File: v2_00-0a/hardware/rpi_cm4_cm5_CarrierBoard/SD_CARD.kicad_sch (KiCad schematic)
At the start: 17 parts, among them J1 DM3AT-SF-PEJM5, Q4 2N7002, Q5 2N7002, Q6 2N7002, U4 AP22913W6-7

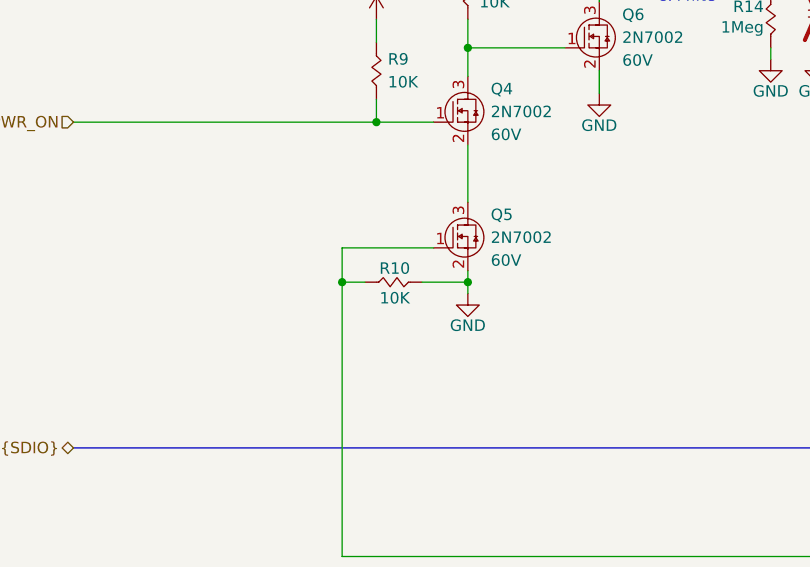
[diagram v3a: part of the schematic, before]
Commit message: Add design notes (power table) and latest changes to power supply and power input
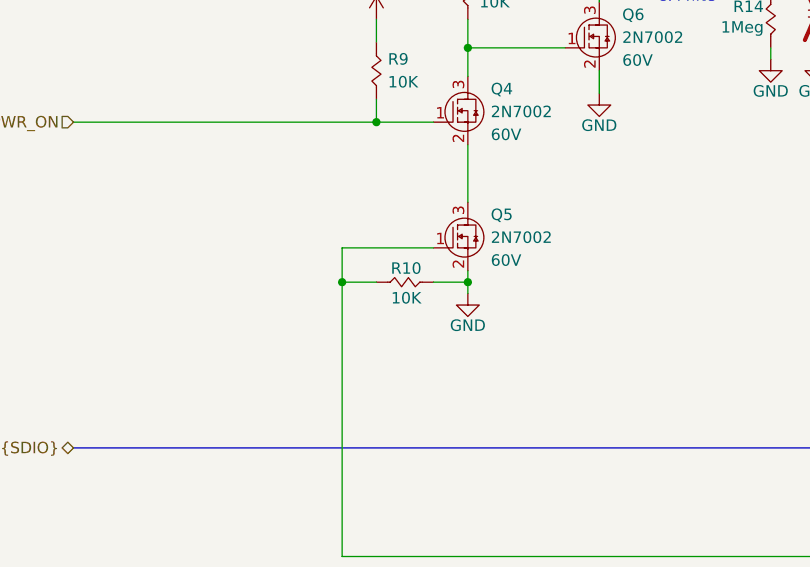
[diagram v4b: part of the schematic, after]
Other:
- moved on the sheet: R10
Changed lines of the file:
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@@
 	(wire
 		(pts
-			(xy 83.185 93.98) (xy 88.265 93.98)
+			(xy 84.455 93.98) (xy 88.265 93.98)
 		)
 		(stroke
@@
 	(wire
 		(pts
-			(xy 74.295 93.98) (xy 76.835 93.98)
+			(xy 74.295 93.98) (xy 78.105 93.98)
 		)
 		(stroke
@@
 	(symbol
 		(lib_id "KicadCompDb:Resistors/RES_SMT_00013")
-		(at 81.915 93.98 180)
+		(at 83.185 93.98 180)
 		(unit 1)
 		(exclude_from_sim no)
@@
 		(dnp no)
 		(property "Reference" "R10"
-			(at 80.137 92.456 0)
+			(at 81.407 92.456 0)
 			(effects
 				(font
@@
 		)
 		(property "Value" "10K"
-			(at 80.137 95.758 0)
+			(at 81.407 95.758 0)
 			(effects
 				(font
@@
 		)
 		(property "Footprint" "footprint:RES_0402"
-			(at 81.407 71.882 0)
+			(at 82.677 71.882 0)
 			(effects
 				(font
@@
 		)
 		(property "Datasheet" "https://www.yageogroup.com/content/datasheet/asset/file/PYU-RC_GROUP_51_ROHS_L"
-			(at 81.915 93.98 0)
+			(at 83.185 93.98 0)
 			(effects
 				(font
@@
 		)
 		(property "Description" "RES 10K OHM 1% 1/16W 0402"
-			(at 80.137 84.074 0)
+			(at 81.407 84.074 0)
 			(effects
 				(font
@@
 		)
 		(property "Tolerance" "1%"
-			(at 81.661 73.66 0)
+			(at 82.931 73.66 0)
 			(effects
 				(font
@@
 		)
 		(property "Power" "1/16W"
-			(at 81.661 79.756 0)
+			(at 82.931 79.756 0)
 			(effects
 				(font
@@
 		)
 		(property "Package" "0402"
-			(at 81.915 77.724 0)
+			(at 83.185 77.724 0)
 			(effects
 				(font
@@
 		)
 		(property "Manufacturer" "YAGEO"
-			(at 81.661 75.692 0)
+			(at 82.931 75.692 0)
 			(effects
 				(font
@@
 		)
 		(property "Manufacturer Part Number" "RC0402FR-0710KL"
-			(at 81.661 86.106 0)
+			(at 82.931 86.106 0)
 			(effects
 				(font
@@
 		)
 		(property "Distributor" "DigiKey"
-			(at 81.915 88.138 0)
+			(at 83.185 88.138 0)
 			(effects
 				(font
@@
 		)
 		(property "Distributor Part Number" "311-10.0KLRCT-ND"
-			(at 81.153 81.788 0)
+			(at 82.423 81.788 0)
 			(effects
 				(font
@@
 		)
 		(property "Temperature Coefficient" "±100ppm/°C"
-			(at 81.915 93.98 0)
+			(at 83.185 93.98 0)
 			(effects
 				(font
@@
 		)
 		(property "Operating Temperature" "-55°C ~ 155°C"
-			(at 81.153 69.596 0)
+			(at 82.423 69.596 0)
 			(effects
 				(font
@@
 		)
 		(property "Type" "RES SMT"
-			(at 81.915 93.98 0)
+			(at 83.185 93.98 0)
 			(show_name yes)
 			(effects
@@
 		)
 		(property "Dimensions" "1.00mm x 0.50mm"
-			(at 81.915 93.98 0)
+			(at 83.185 93.98 0)
 			(show_name yes)
 			(effects
